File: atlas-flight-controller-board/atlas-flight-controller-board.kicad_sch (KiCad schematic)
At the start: 0 parts

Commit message: testing vcs within kicad.
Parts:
- added C1: C, symbol Device:C
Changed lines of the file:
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@@
 	(generator_version "9.0")
 	(paper "A4")
+	(symbol
+		(lib_id "Device:C")
+		(at 63.5 50.8 0)
+		(unit 1)
+		(exclude_from_sim no)
+		(in_bom yes)
+		(on_board yes)
+		(dnp no)
+		(fields_autoplaced yes)
+		(property "Reference" "C1"
+			(at 67.31 49.5299 0)
+			(effects
+				(font
+					(size 1.27 1.27)
+				)
+				(justify left)
+			)
+		)
+		(property "Value" "C"
+			(at 67.31 52.0699 0)
+			(effects
+				(font
+					(size 1.27 1.27)
+				)
+				(justify left)
+			)
+		)
+		(property "Footprint" ""
+			(at 64.4652 54.61 0)
+			(effects
+				(font
+					(size 1.27 1.27)
+				)
+				(hide yes)
+			)
+		)
+		(property "Datasheet" "~"
+			(at 63.5 50.8 0)
+			(effects
+				(font
+					(size 1.27 1.27)
+				)
+				(hide yes)
+			)
+		)
+		(property "Description" "Unpolarized capacitor"
+			(at 63.5 50.8 0)
+			(effects
+				(font
+					(size 1.27 1.27)
+				)
+				(hide yes)
+			)
+		)
+		(pin "1"
+		)
+		(pin "2"
+		)
+		(instances
+			(project ""
+				(path "/99efb2d6-b5f7-438c-9ed2-f359400f01a1"
+					(reference "C1")
+					(unit 1)
+				)
+			)
+		)
+	)
 	(sheet_instances
 		(path "/"

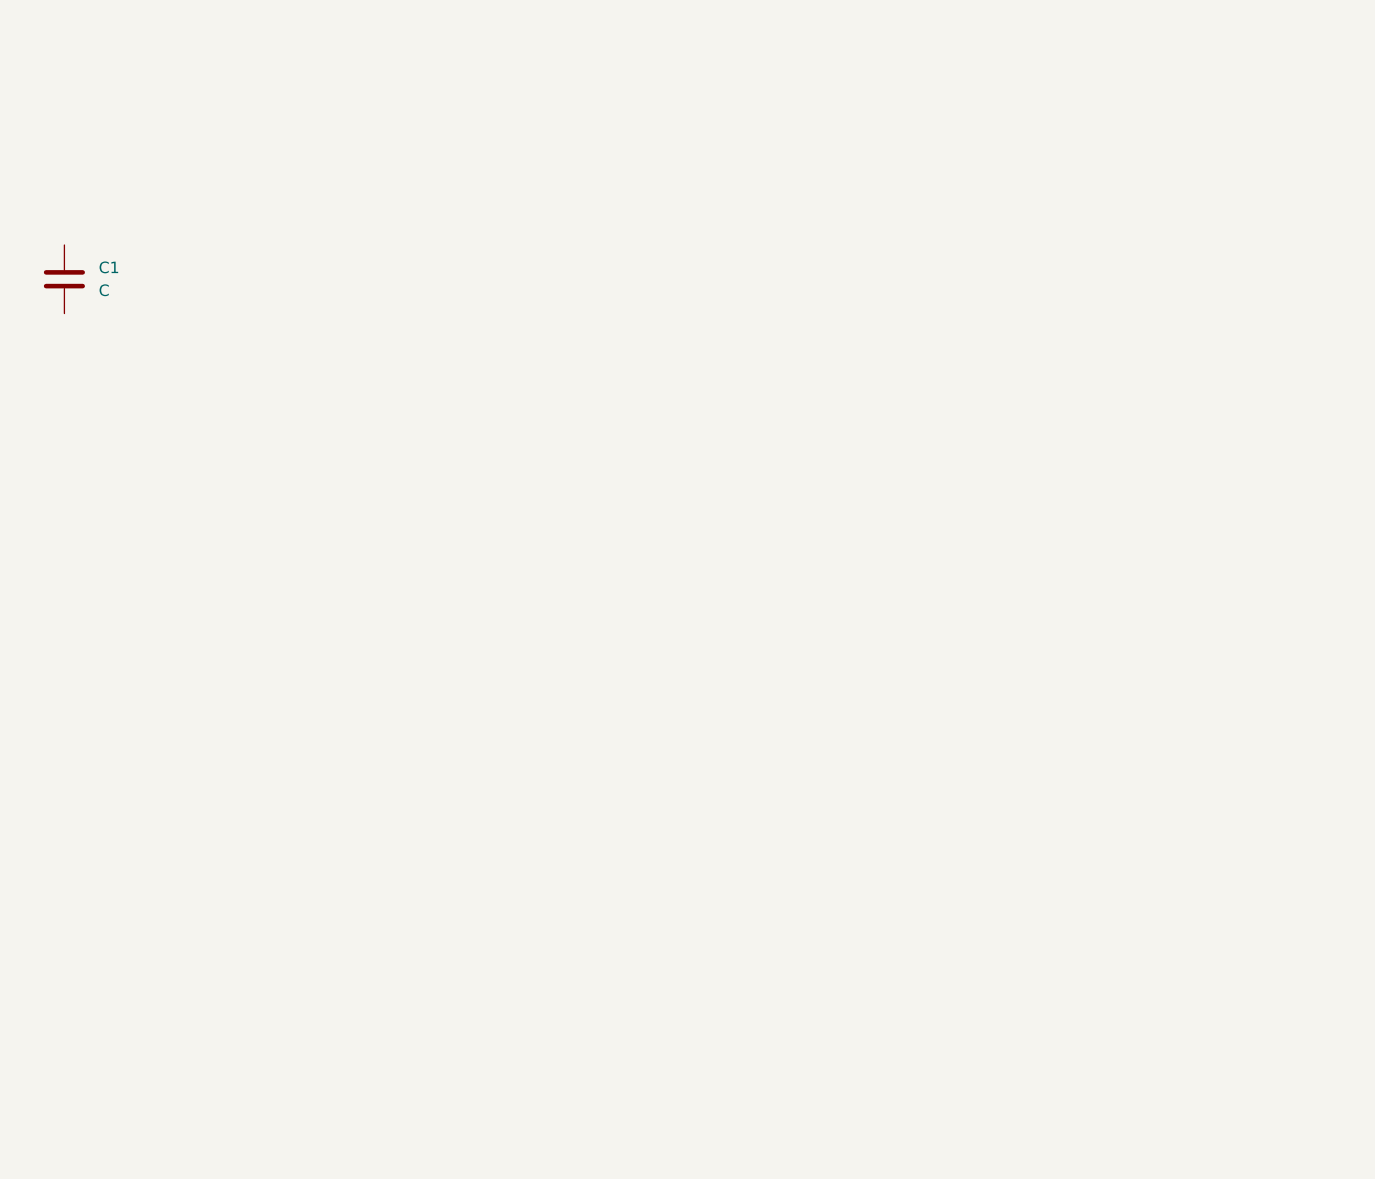
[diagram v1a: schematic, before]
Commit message: Added Hierarchical Sheets. Finished IMU Schematic.
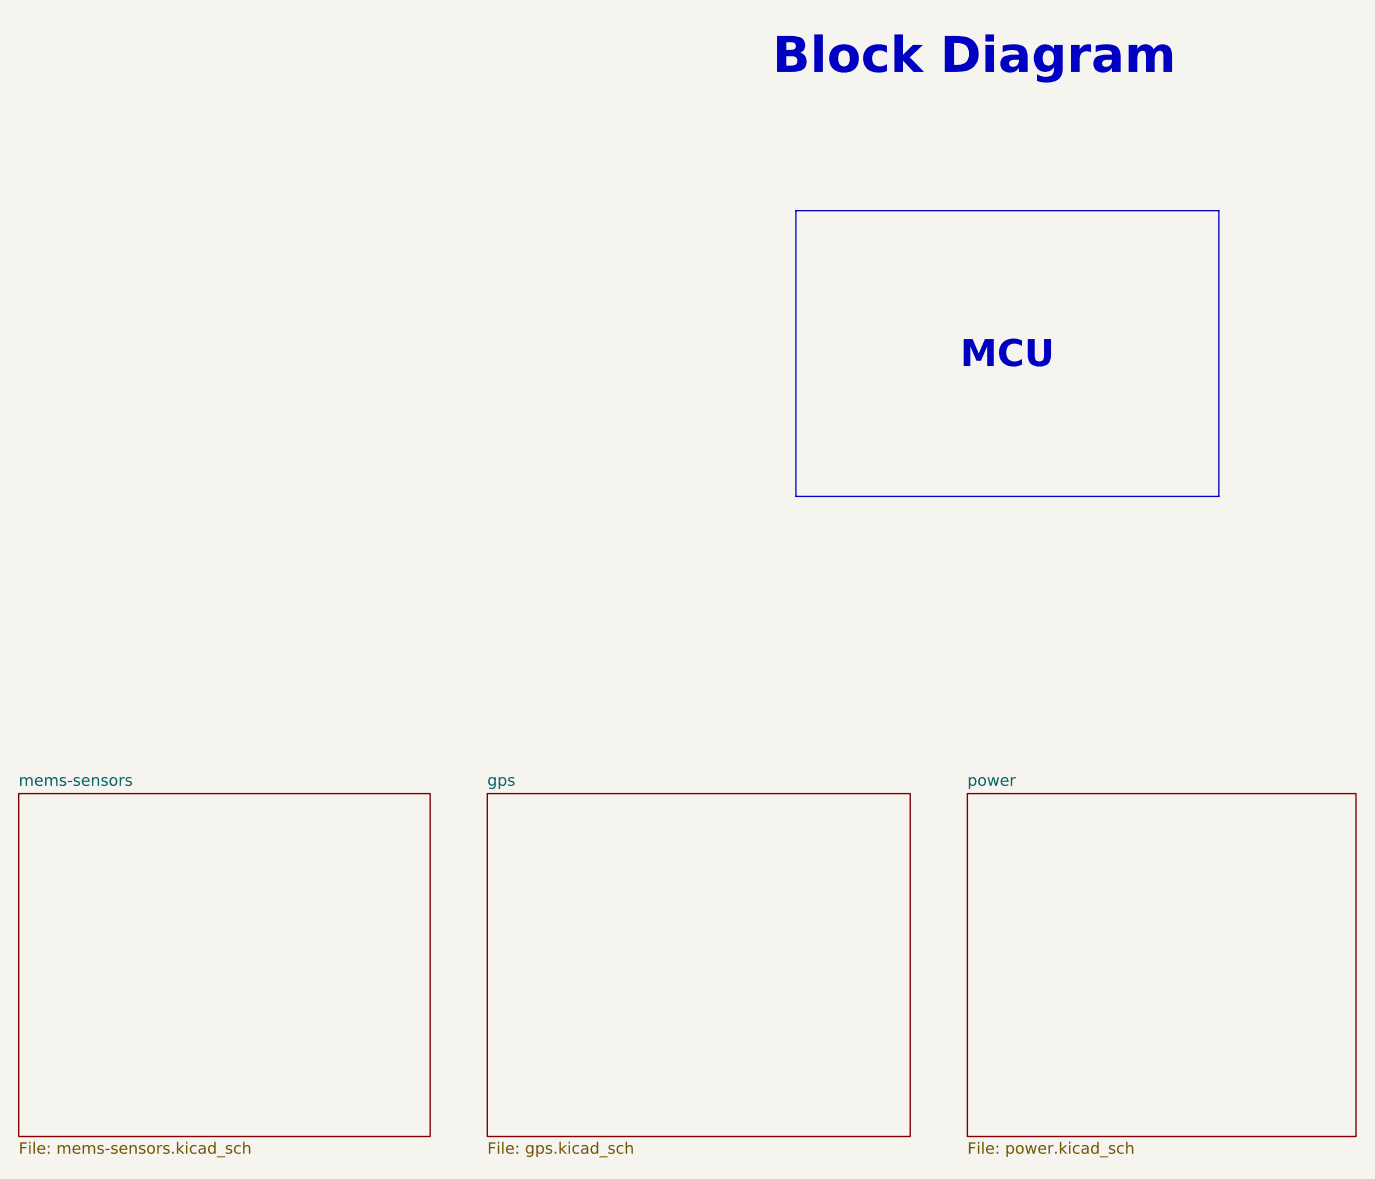
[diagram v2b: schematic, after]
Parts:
- removed C1: C, symbol Device:C
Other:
- added sheet gps (gps.kicad_sch)
- added sheet mems-sensors (mems-sensors.kicad_sch)
- added sheet power (power.kicad_sch)
- note added: "Block Diagram"
- company: (none) -> ARCUIA
- title: (none) -> Top Page
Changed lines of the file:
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@@
 	(generator_version "9.0")
 	(paper "A4")
-	(symbol
-		(lib_id "Device:C")
-		(at 63.5 50.8 0)
-		(unit 1)
+	(title_block
+		(title "Top Page")
+		(rev "v1.0")
+		(company "ARCUIA")
+	)
+	(text "Block Diagram"
+		(exclude_from_sim no)
+		(at 164.592 26.162 0)
+		(effects
+			(font
+				(size 4 4)
+				(thickness 0.8)
+				(bold yes)
+			)
+		)
+	)
+	(text_box "MCU"
+		(exclude_from_sim no)
+		(at 144.78 43.18 0)
+		(size 46.99 31.75)
+		(margins 0.9525 0.9525 0.9525 0.9525)
+		(stroke
+			(width 0)
+			(type solid)
+		)
+		(fill
+			(type color)
+			(color 0 255 255 1)
+		)
+		(effects
+			(font
+				(size 3 3)
+				(thickness 0.254)
+				(bold yes)
+			)
+		)
+	)
+	(sheet
+		(at 58.42 107.95)
+		(size 45.72 38.1)
 		(exclude_from_sim no)
 		(in_bom yes)
@@
 		(dnp no)
 		(fields_autoplaced yes)
-		(property "Reference" "C1"
-			(at 67.31 49.5299 0)
+		(stroke
+			(width 0.1524)
+			(type solid)
+		)
+		(fill
+			(color 194 194 194 1.0000)
+		)
+		(property "Sheetname" "mems-sensors"
+			(at 58.42 107.2384 0)
+			(show_name yes)
 			(effects
 				(font
 					(size 1.27 1.27)
 				)
-				(justify left)
+				(justify left bottom)
 			)
 		)
-		(property "Value" "C"
-			(at 67.31 52.0699 0)
+		(property "Sheetfile" "mems-sensors.kicad_sch"
+			(at 58.42 146.6346 0)
 			(effects
 				(font
 					(size 1.27 1.27)
 				)
-				(justify left)
+				(justify left top)
 			)
 		)
-		(property "Footprint" ""
-			(at 64.4652 54.61 0)
+		(instances
+			(project "atlas-flight-controller-board"
+				(path "/99efb2d6-b5f7-438c-9ed2-f359400f01a1"
+					(page "2")
+				)
+			)
+		)
+	)
+	(sheet
+		(at 110.49 107.95)
+		(size 46.99 38.1)
+		(exclude_from_sim no)
+		(in_bom yes)
+		(on_board yes)
+		(dnp no)
+		(fields_autoplaced yes)
+		(stroke
+			(width 0.1524)
+			(type solid)
+		)
+		(fill
+			(color 194 194 194 1.0000)
+		)
+		(property "Sheetname" "gps"
+			(at 110.49 107.2384 0)
+			(show_name yes)
 			(effects
 				(font
 					(size 1.27 1.27)
 				)
-				(hide yes)
+				(justify left bottom)
 			)
 		)
-		(property "Datasheet" "~"
-			(at 63.5 50.8 0)
+		(property "Sheetfile" "gps.kicad_sch"
+			(at 110.49 146.6346 0)
 			(effects
 				(font
 					(size 1.27 1.27)
 				)
-				(hide yes)
+				(justify left top)
 			)
 		)
-		(property "Description" "Unpolarized capacitor"
-			(at 63.5 50.8 0)
+		(instances
+			(project "atlas-flight-controller-board"
+				(path "/99efb2d6-b5f7-438c-9ed2-f359400f01a1"
+					(page "3")
+				)
+			)
+		)
+	)
+	(sheet
+		(at 163.83 107.95)
+		(size 43.18 38.1)
+		(exclude_from_sim no)
+		(in_bom yes)
+		(on_board yes)
+		(dnp no)
+		(fields_autoplaced yes)
+		(stroke
+			(width 0.1524)
+			(type solid)
+		)
+		(fill
+			(color 194 194 194 1.0000)
+		)
+		(property "Sheetname" "power"
+			(at 163.83 107.2384 0)
+			(show_name yes)
 			(effects
 				(font
 					(size 1.27 1.27)
 				)
-				(hide yes)
+				(justify left bottom)
 			)
 		)
-		(pin "1"
-		)
-		(pin "2"
+		(property "Sheetfile" "power.kicad_sch"
+			(at 163.83 146.6346 0)
+			(effects
+				(font
+					(size 1.27 1.27)
+				)
+				(justify left top)
+			)
 		)
 		(instances
-			(project ""
+			(project "atlas-flight-controller-board"
 				(path "/99efb2d6-b5f7-438c-9ed2-f359400f01a1"
-					(reference "C1")
-					(unit 1)
+					(page "4")
 				)
 			)

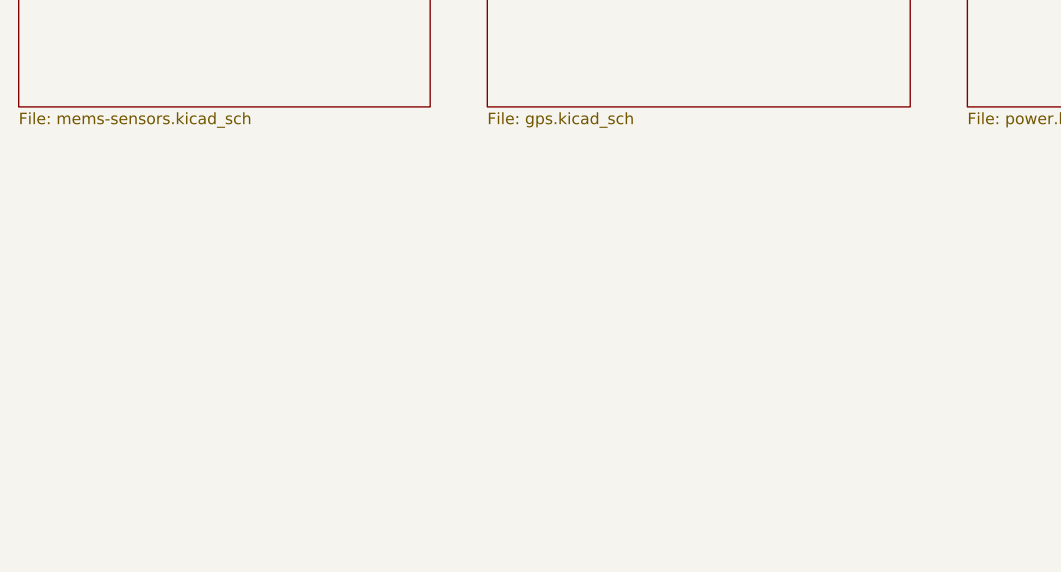
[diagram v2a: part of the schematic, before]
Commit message: wip commit, adding tennsy 4.1 and sd card.
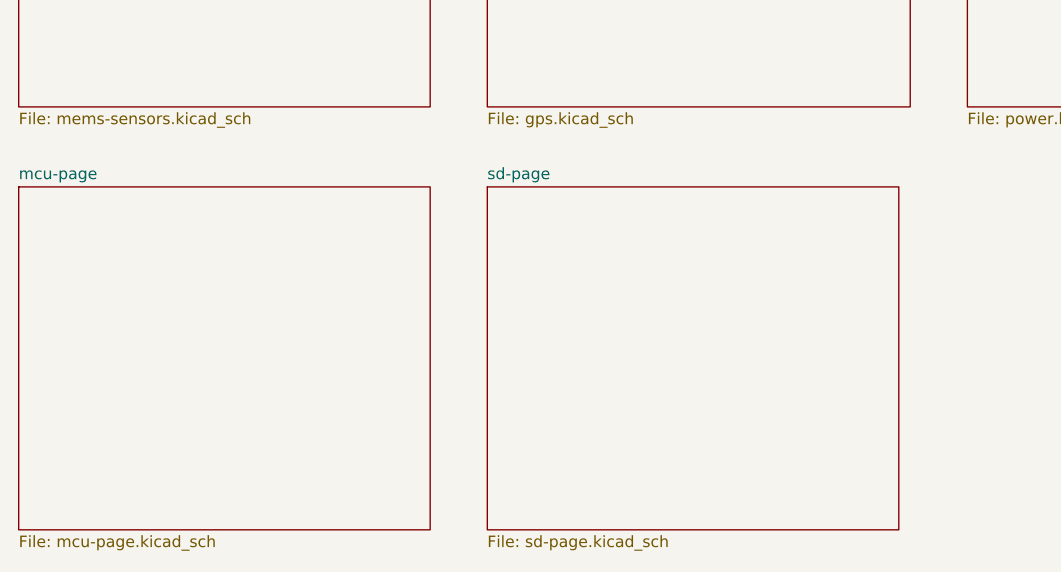
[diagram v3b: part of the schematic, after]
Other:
- added sheet mcu-page (mcu-page.kicad_sch)
- added sheet sd-page (sd-page.kicad_sch)
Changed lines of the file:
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@@
+	)
+	(sheet
+		(at 110.49 154.94)
+		(size 45.72 38.1)
+		(exclude_from_sim no)
+		(in_bom yes)
+		(on_board yes)
+		(dnp no)
+		(fields_autoplaced yes)
+		(stroke
+			(width 0.1524)
+			(type solid)
+		)
+		(fill
+			(color 194 194 194 1.0000)
+		)
+		(property "Sheetname" "sd-page"
+			(at 110.49 154.2284 0)
+			(show_name yes)
+			(effects
+				(font
+					(size 1.27 1.27)
+				)
+				(justify left bottom)
+			)
+		)
+		(property "Sheetfile" "sd-page.kicad_sch"
+			(at 110.49 193.6246 0)
+			(effects
+				(font
+					(size 1.27 1.27)
+				)
+				(justify left top)
+			)
+		)
+		(instances
+			(project "atlas-flight-controller-board"
+				(path "/99efb2d6-b5f7-438c-9ed2-f359400f01a1"
+					(page "6")
+				)
+			)
+		)
 	)
 	(sheet
@@
 				)
 			)
+		)
+	)
+	(sheet
+		(at 58.42 154.94)
+		(size 45.72 38.1)
+		(exclude_from_sim no)
+		(in_bom yes)
+		(on_board yes)
+		(dnp no)
+		(fields_autoplaced yes)
+		(stroke
+			(width 0.1524)
+			(type solid)
+		)
+		(fill
+			(color 194 194 194 1.0000)
+		)
+		(property "Sheetname" "mcu-page"
+			(at 58.42 154.2284 0)
+			(show_name yes)
+			(effects
+				(font
+					(size 1.27 1.27)
+				)
+				(justify left bottom)
+			)
+		)
+		(property "Sheetfile" "mcu-page.kicad_sch"
+			(at 58.42 193.6246 0)
+			(effects
+				(font
+					(size 1.27 1.27)
+				)
+				(justify left top)
+			)
+		)
+		(instances
+			(project "atlas-flight-controller-board"
+				(path "/99efb2d6-b5f7-438c-9ed2-f359400f01a1"
+					(page "5")
+				)
+			)

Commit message: finishing up schematic for v1.
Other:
- added sheet radio-page (radio-page.kicad_sch)
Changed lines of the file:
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@@
 	(text "Block Diagram"
 		(exclude_from_sim no)
-		(at 164.592 26.162 0)
+		(at 247.142 23.368 0)
 		(effects
 			(font
@@
 	(text_box "MCU"
 		(exclude_from_sim no)
-		(at 144.78 43.18 0)
+		(at 224.79 33.02 0)
 		(size 46.99 31.75)
 		(margins 0.9525 0.9525 0.9525 0.9525)
@@
 	)
 	(sheet
-		(at 110.49 154.94)
+		(at 73.66 68.58)
 		(size 45.72 38.1)
 		(exclude_from_sim no)
@@
 		)
 		(property "Sheetname" "sd-page"
-			(at 110.49 154.2284 0)
+			(at 73.66 67.8684 0)
 			(show_name yes)
 			(effects
@@
 		)
 		(property "Sheetfile" "sd-page.kicad_sch"
-			(at 110.49 193.6246 0)
+			(at 73.66 107.2646 0)
 			(effects
 				(font
@@
 	)
 	(sheet
-		(at 58.42 107.95)
+		(at 127 68.58)
+		(size 45.72 38.1)
+		(exclude_from_sim no)
+		(in_bom yes)
+		(on_board yes)
+		(dnp no)
+		(fields_autoplaced yes)
+		(stroke
+			(width 0.1524)
+			(type solid)
+		)
+		(fill
+			(color 194 194 194 1.0000)
+		)
+		(property "Sheetname" "radio-page"
+			(at 127 67.8684 0)
+			(show_name yes)
+			(effects
+				(font
+					(size 1.27 1.27)
+				)
+				(justify left bottom)
+			)
+		)
+		(property "Sheetfile" "radio-page.kicad_sch"
+			(at 127 107.2646 0)
+			(effects
+				(font
+					(size 1.27 1.27)
+				)
+				(justify left top)
+			)
+		)
+		(instances
+			(project "atlas-flight-controller-board"
+				(path "/99efb2d6-b5f7-438c-9ed2-f359400f01a1"
+					(page "7")
+				)
+			)
+		)
+	)
+	(sheet
+		(at 21.59 21.59)
 		(size 45.72 38.1)
 		(exclude_from_sim no)
@@
 		)
 		(property "Sheetname" "mems-sensors"
-			(at 58.42 107.2384 0)
+			(at 21.59 20.8784 0)
 			(show_name yes)
 			(effects
@@
 		)
 		(property "Sheetfile" "mems-sensors.kicad_sch"
-			(at 58.42 146.6346 0)
+			(at 21.59 60.2746 0)
 			(effects
 				(font
@@
 	)
 	(sheet
-		(at 110.49 107.95)
+		(at 73.66 21.59)
 		(size 46.99 38.1)
 		(exclude_from_sim no)
@@
 		)
 		(property "Sheetname" "gps"
-			(at 110.49 107.2384 0)
+			(at 73.66 20.8784 0)
 			(show_name yes)
 			(effects
@@
 		)
 		(property "Sheetfile" "gps.kicad_sch"
-			(at 110.49 146.6346 0)
+			(at 73.66 60.2746 0)
 			(effects
 				(font
@@
 	)
 	(sheet
-		(at 163.83 107.95)
+		(at 127 21.59)
 		(size 43.18 38.1)
 		(exclude_from_sim no)
@@
 		)
 		(property "Sheetname" "power"
-			(at 163.83 107.2384 0)
+			(at 127 20.8784 0)
 			(show_name yes)
 			(effects
@@
 		)
 		(property "Sheetfile" "power.kicad_sch"
-			(at 163.83 146.6346 0)
+			(at 127 60.2746 0)
 			(effects
 				(font
@@
 	)
 	(sheet
-		(at 58.42 154.94)
+		(at 21.59 68.58)
 		(size 45.72 38.1)
 		(exclude_from_sim no)
@@
 		)
 		(property "Sheetname" "mcu-page"
-			(at 58.42 154.2284 0)
+			(at 21.59 67.8684 0)
 			(show_name yes)
 			(effects
@@
 		)
 		(property "Sheetfile" "mcu-page.kicad_sch"
-			(at 58.42 193.6246 0)
-			(effects
-				(font
+			(at 21.59 107.2646 0)
+			(effects
+				(font

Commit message: wip commit
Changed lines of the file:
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@@
 	)
 	(sheet
-		(at 127 68.58)
+		(at 125.73 68.58)
 		(size 45.72 38.1)
 		(exclude_from_sim no)
@@
 		)
 		(property "Sheetname" "radio-page"
-			(at 127 67.8684 0)
+			(at 125.73 67.8684 0)
 			(show_name yes)
 			(effects
@@
 		)
 		(property "Sheetfile" "radio-page.kicad_sch"
-			(at 127 107.2646 0)
+			(at 125.73 107.2646 0)
 			(effects
 				(font
@@
 	(sheet
 		(at 73.66 21.59)
-		(size 46.99 38.1)
+		(size 45.72 38.1)
 		(exclude_from_sim no)
 		(in_bom yes)
@@
 	)
 	(sheet
-		(at 127 21.59)
-		(size 43.18 38.1)
+		(at 125.73 21.59)
+		(size 45.72 38.1)
 		(exclude_from_sim no)
 		(in_bom yes)
@@
 		)
 		(property "Sheetname" "power"
-			(at 127 20.8784 0)
+			(at 125.73 20.8784 0)
 			(show_name yes)
 			(effects
@@
 		)
 		(property "Sheetfile" "power.kicad_sch"
-			(at 127 60.2746 0)
+			(at 125.73 60.2746 0)
 			(effects
 				(font
